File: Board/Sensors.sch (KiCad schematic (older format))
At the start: 14 parts, among them Q6 IRLML6344TRPBF

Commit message: Some corrections.
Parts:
- R32: value 51k -> 22.1k
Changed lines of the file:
@@
 P 2750 3850
 F 0 "R32" H 2820 3896 50  0000 L CNN
-F 1 "51k" H 2820 3805 50  0000 L CNN
+F 1 "22.1k" H 2820 3805 50  0000 L CNN
 F 2 "Resistor_SMD:R_0603_1608Metric_Pad1.05x0.95mm_HandSolder" V 2680 3850 50  0001 C CNN
 F 3 "~" H 2750 3850 50  0001 C CNN

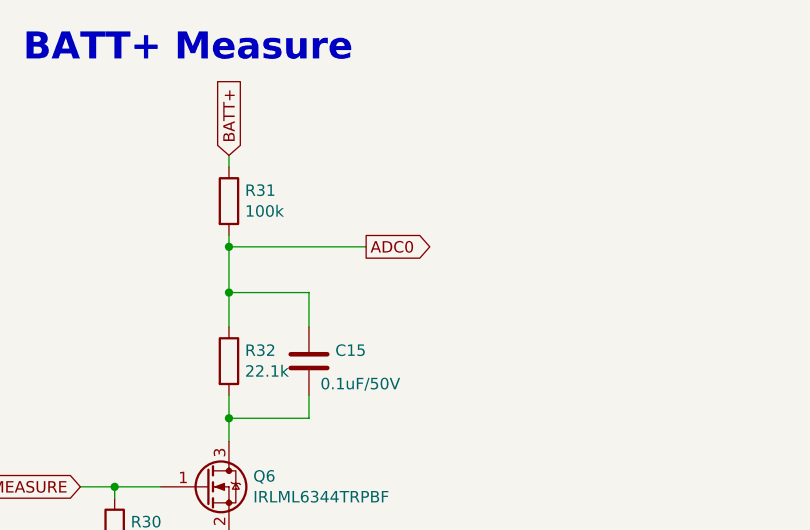
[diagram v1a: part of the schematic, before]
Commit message: MAJOR CORRECTION: moved ADCs to correct port on xmega. Added a LED controlled by the xmega.
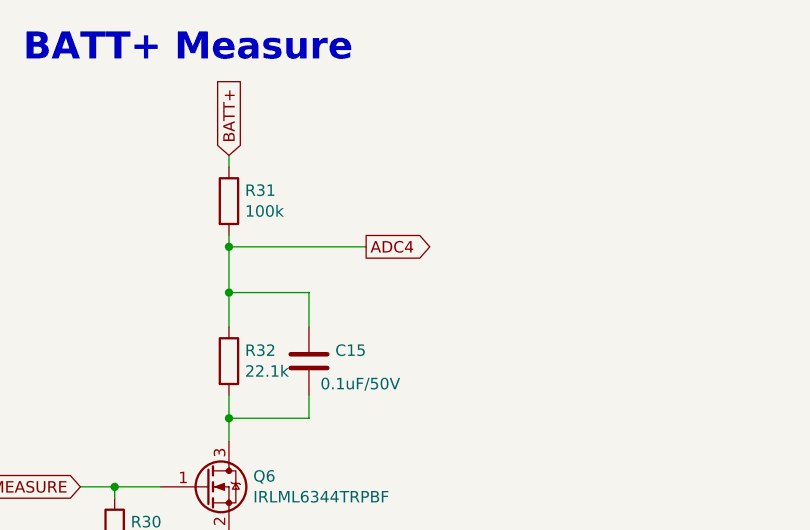
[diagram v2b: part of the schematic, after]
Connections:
- net ADC0 renamed ADC4
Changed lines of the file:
@@
 BATT+
 Text GLabel 3350 3350 2    50   Output ~ 0
-ADC0
+ADC4
 Wire Wire Line
 	2250 4800 2750 4800
